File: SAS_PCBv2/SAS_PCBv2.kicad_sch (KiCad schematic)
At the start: 1 part, among them J2 GPIO_CONNECTOR

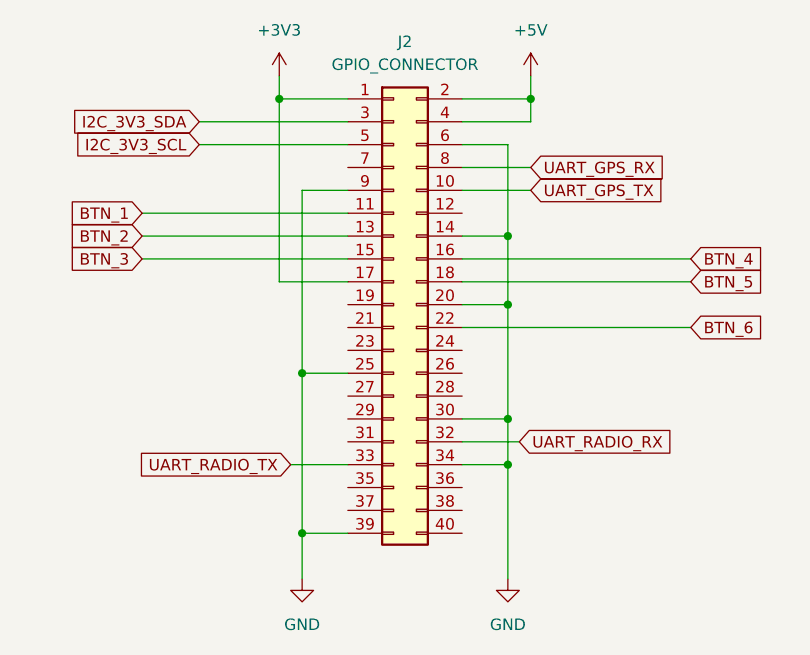
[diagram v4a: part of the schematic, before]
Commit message: schematic sans error et le debut de pcb
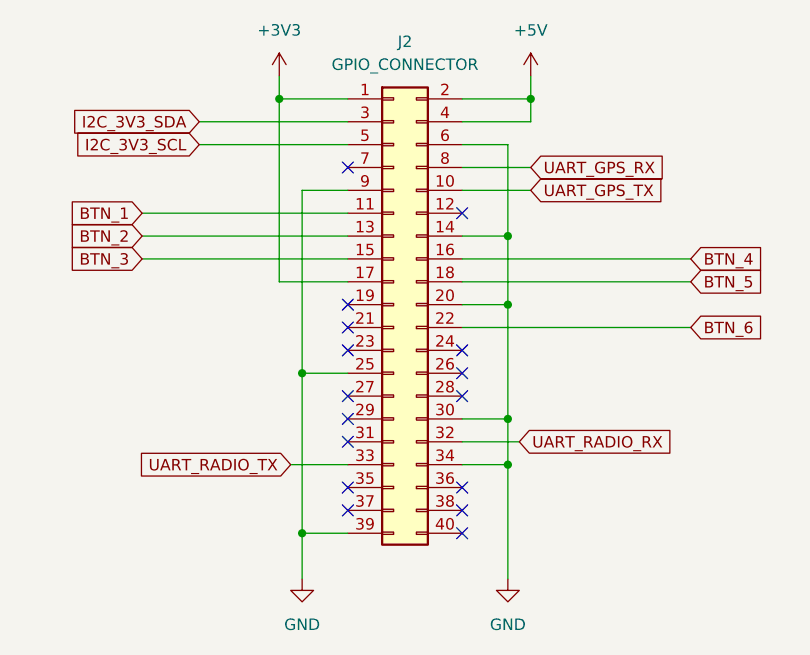
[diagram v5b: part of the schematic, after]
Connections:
- no-connect marks 0 -> 16
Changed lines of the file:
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@@
 		(color 0 0 0 0)
+	)
+	(no_connect
+		(at 179.07 114.3)
+	)
+	(no_connect
+		(at 166.37 88.9)
+	)
+	(no_connect
+		(at 166.37 114.3)
+	)
+	(no_connect
+		(at 179.07 129.54)
+	)
+	(no_connect
+		(at 166.37 119.38)
+	)
+	(no_connect
+		(at 166.37 124.46)
+	)
+	(no_connect
+		(at 166.37 106.68)
+	)
+	(no_connect
+		(at 179.07 124.46)
+	)
+	(no_connect
+		(at 179.07 111.76)
+	)
+	(no_connect
+		(at 179.07 93.98)
+	)
+	(no_connect
+		(at 179.07 109.22)
+	)
+	(no_connect
+		(at 166.37 109.22)
+	)
+	(no_connect
+		(at 166.37 104.14)
+	)
+	(no_connect
+		(at 166.37 116.84)
+	)
+	(no_connect
+		(at 179.07 127)
+	)
+	(no_connect
+		(at 166.37 127)
 	)
 	(wire

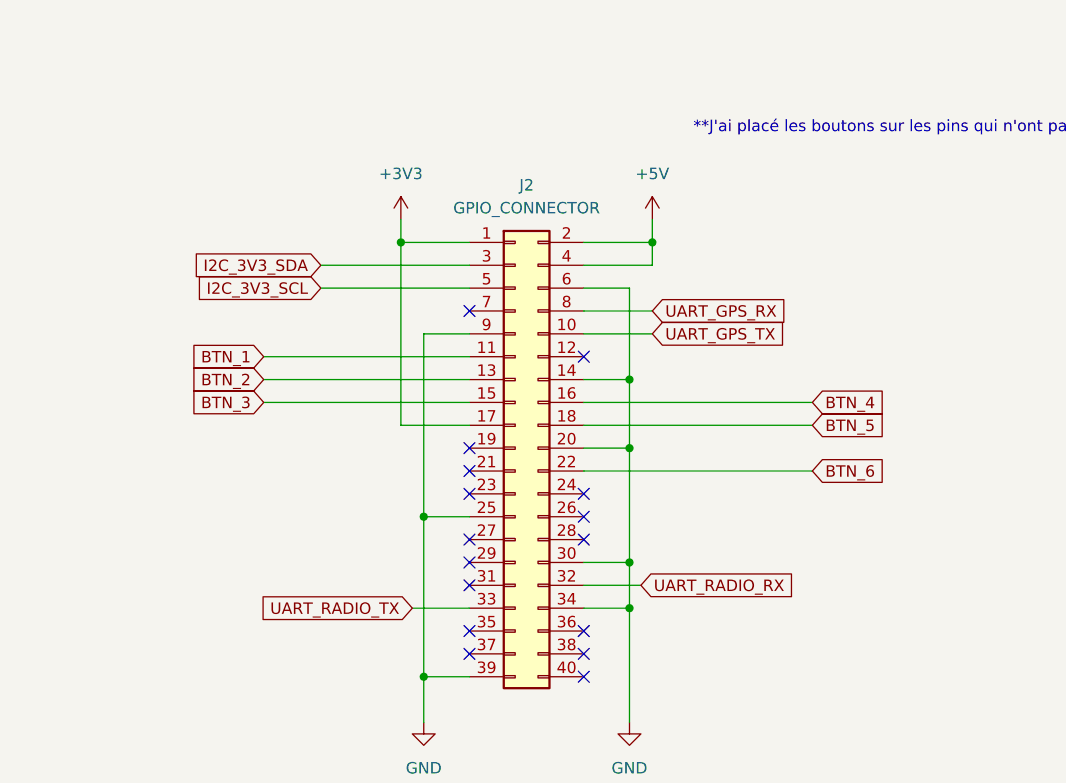
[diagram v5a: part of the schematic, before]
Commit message: Correction UART5 -> UART3, ajout d'un ventilateur 12V PWM
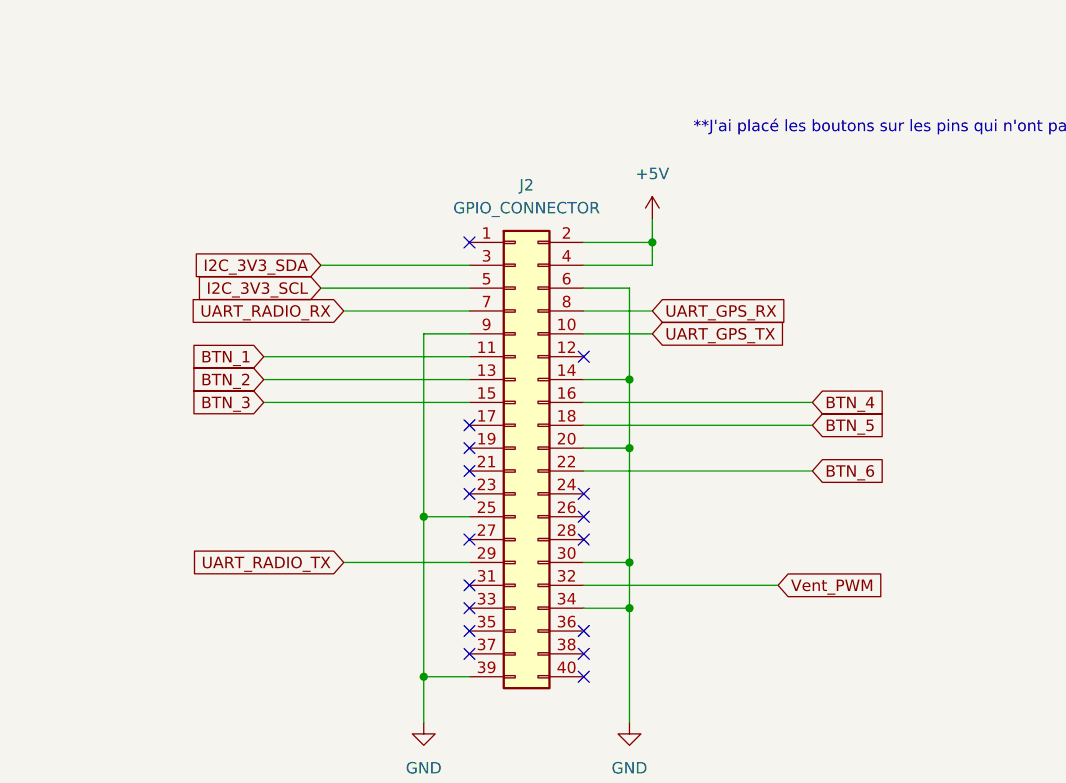
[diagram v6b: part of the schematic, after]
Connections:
- net UART_RADIO_RX: now also J2.7 (Pin_7); no longer J2.32 (Pin_32)
- net UART_RADIO_TX: now also J2.29 (Pin_29); no longer J2.33 (Pin_33)
- net +3V3: no longer names the net of J2.1 (Pin_1)
- net +3V3: no longer J2.17 (Pin_17)
- new net Vent_PWM: J2.32 (Pin_32)
- no-connect marks 16 -> 17
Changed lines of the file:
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@@
 		(color 0 0 0 0)
 	)
-	(junction
-		(at 158.75 81.28)
-		(diameter 0)
-		(color 0 0 0 0)
-	)
 	(no_connect
 		(at 179.07 114.3)
 	)
 	(no_connect
-		(at 166.37 88.9)
-	)
-	(no_connect
 		(at 166.37 114.3)
 	)
@@
 	)
 	(no_connect
-		(at 166.37 116.84)
+		(at 166.37 81.28)
+	)
+	(no_connect
+		(at 166.37 101.6)
 	)
 	(no_connect
@@
 	)
 	(no_connect
+		(at 166.37 121.92)
+	)
+	(no_connect
 		(at 166.37 127)
 	)
@@
 	(wire
 		(pts
-			(xy 160.02 121.92) (xy 166.37 121.92)
-		)
-		(stroke
-			(width 0)
-			(type default)
-		)
-	)
-	(wire
-		(pts
 			(xy 179.07 104.14) (xy 184.15 104.14)
 		)
@@
 	(wire
 		(pts
-			(xy 158.75 81.28) (xy 166.37 81.28)
-		)
-		(stroke
-			(width 0)
-			(type default)
-		)
-	)
-	(wire
-		(pts
 			(xy 149.86 86.36) (xy 166.37 86.36)
 		)
@@
 	(wire
 		(pts
-			(xy 158.75 81.28) (xy 158.75 101.6)
-		)
-		(stroke
-			(width 0)
-			(type default)
-		)
-	)
-	(wire
-		(pts
 			(xy 161.29 111.76) (xy 166.37 111.76)
 		)
@@
 	(wire
 		(pts
+			(xy 152.4 116.84) (xy 166.37 116.84)
+		)
+		(stroke
+			(width 0)
+			(type default)
+		)
+	)
+	(wire
+		(pts
 			(xy 184.15 96.52) (xy 184.15 104.14)
 		)
@@
 	(wire
 		(pts
+			(xy 152.4 88.9) (xy 166.37 88.9)
+		)
+		(stroke
+			(width 0)
+			(type default)
+		)
+	)
+	(wire
+		(pts
 			(xy 161.29 111.76) (xy 161.29 129.54)
 		)
@@
 	(wire
 		(pts
-			(xy 166.37 101.6) (xy 158.75 101.6)
-		)
-		(stroke
-			(width 0)
-			(type default)
-		)
-	)
-	(wire
-		(pts
-			(xy 158.75 78.74) (xy 158.75 81.28)
-		)
-		(stroke
-			(width 0)
-			(type default)
-		)
-	)
-	(wire
-		(pts
 			(xy 143.51 99.06) (xy 166.37 99.06)
 		)
@@
 	(wire
 		(pts
-			(xy 179.07 119.38) (xy 185.42 119.38)
-		)
-		(stroke
-			(width 0)
-			(type default)
-		)
-	)
-	(wire
-		(pts
 			(xy 184.15 121.92) (xy 184.15 134.62)
 		)
@@
 	(wire
 		(pts
+			(xy 179.07 119.38) (xy 200.66 119.38)
+		)
+		(stroke
+			(width 0)
+			(type default)
+		)
+	)
+	(wire
+		(pts
 			(xy 179.07 99.06) (xy 204.47 99.06)
 		)
@@
 	(global_label "UART_RADIO_RX"
 		(shape input)
-		(at 185.42 119.38 0)
+		(at 152.4 88.9 180)
+		(fields_autoplaced yes)
+		(effects
+			(font
+				(size 1.27 1.27)
+			)
+			(justify right)
+		)
+		(property "Intersheetrefs" "${INTERSHEET_REFS}"
+			(at 134.7795 88.9 0)
+			(effects
+				(font
+					(size 1.27 1.27)
+				)
+				(justify right)
+				(hide yes)
+			)
+		)
+	)
+	(global_label "BTN_3"
+		(shape input)
+		(at 143.51 99.06 180)
+		(fields_autoplaced yes)
+		(effects
+			(font
+				(size 1.27 1.27)
+			)
+			(justify right)
+		)
+		(property "Intersheetrefs" "${INTERSHEET_REFS}"
+			(at 134.7796 99.06 0)
+			(effects
+				(font
+					(size 1.27 1.27)
+				)
+				(justify right)
+				(hide yes)
+			)
+		)
+	)
+	(global_label "UART_RADIO_TX"
+		(shape input)
+		(at 152.4 116.84 180)
+		(fields_autoplaced yes)
+		(effects
+			(font
+				(size 1.27 1.27)
+			)
+			(justify right)
+		)
+		(property "Intersheetrefs" "${INTERSHEET_REFS}"
+			(at 135.0819 116.84 0)
+			(effects
+				(font
+					(size 1.27 1.27)
+				)
+				(justify right)
+				(hide yes)
+			)
+		)
+	)
+	(global_label "BTN_5"
+		(shape input)
+		(at 204.47 101.6 0)
 		(fields_autoplaced yes)
 		(effects
@@
 		)
 		(property "Intersheetrefs" "${INTERSHEET_REFS}"
-			(at 203.0405 119.38 0)
+			(at 213.2004 101.6 0)
 			(effects
 				(font
@@
 		)
 	)
-	(global_label "BTN_3"
-		(shape input)
-		(at 143.51 99.06 180)
+	(global_label "BTN_1"
+		(shape input)
+		(at 143.51 93.98 180)
 		(fields_autoplaced yes)
 		(effects
@@
 		)
 		(property "Intersheetrefs" "${INTERSHEET_REFS}"
-			(at 134.7796 99.06 0)
+			(at 134.7796 93.98 0)
 			(effects
 				(font
@@
 		)
 	)
-	(global_label "UART_RADIO_TX"
-		(shape input)
-		(at 160.02 121.92 180)
+	(global_label "I2C_3V3_SDA"
+		(shape input)
+		(at 149.86 83.82 180)
 		(fields_autoplaced yes)
 		(effects
@@
 		)
 		(property "Intersheetrefs" "${INTERSHEET_REFS}"
-			(at 142.7019 121.92 0)
+			(at 134.7796 83.82 0)
 			(effects
 				(font
@@
 		)
 	)
-	(global_label "BTN_5"
-		(shape input)
-		(at 204.47 101.6 0)
+	(global_label "BTN_2"
+		(shape input)
+		(at 143.51 96.52 180)
+		(fields_autoplaced yes)
+		(effects
+			(font
+				(size 1.27 1.27)
+			)
+			(justify right)
+		)
+		(property "Intersheetrefs" "${INTERSHEET_REFS}"
+			(at 134.7796 96.52 0)
+			(effects
+				(font
+					(size 1.27 1.27)
+				)
+				(justify right)
+				(hide yes)
+			)
+		)
+	)
+	(global_label "Vent_PWM"
+		(shape input)
+		(at 200.66 119.38 0)
 		(fields_autoplaced yes)
 		(effects
@@
 		)
 		(property "Intersheetrefs" "${INTERSHEET_REFS}"
-			(at 213.2004 101.6 0)
+			(at 214.4704 119.38 0)
 			(effects
 				(font
@@
 				)
 				(justify left)
-				(hide yes)
-			)
-		)
-	)
-	(global_label "BTN_1"
-		(shape input)
-		(at 143.51 93.98 180)
-		(fields_autoplaced yes)
-		(effects
-			(font
-				(size 1.27 1.27)
-			)
-			(justify right)
-		)
-		(property "Intersheetrefs" "${INTERSHEET_REFS}"
-			(at 134.7796 93.98 0)
-			(effects
-				(font
-					(size 1.27 1.27)
-				)
-				(justify right)
-				(hide yes)
-			)
-		)
-	)
-	(global_label "I2C_3V3_SDA"
-		(shape input)
-		(at 149.86 83.82 180)
-		(fields_autoplaced yes)
-		(effects
-			(font
-				(size 1.27 1.27)
-			)
-			(justify right)
-		)
-		(property "Intersheetrefs" "${INTERSHEET_REFS}"
-			(at 134.7796 83.82 0)
-			(effects
-				(font
-					(size 1.27 1.27)
-				)
-				(justify right)
-				(hide yes)
-			)
-		)
-	)
-	(global_label "BTN_2"
-		(shape input)
-		(at 143.51 96.52 180)
-		(fields_autoplaced yes)
-		(effects
-			(font
-				(size 1.27 1.27)
-			)
-			(justify right)
-		)
-		(property "Intersheetrefs" "${INTERSHEET_REFS}"
-			(at 134.7796 96.52 0)
-			(effects
-				(font
-					(size 1.27 1.27)
-				)
-				(justify right)
 				(hide yes)
 			)
@@
 					(unit 1)
 				)
-			)
-		)
-	)
-	(symbol
-		(lib_id "power:+3V3")
-		(at 158.75 78.74 0)
-		(unit 1)
-		(exclude_from_sim no)
-		(in_bom yes)
-		(on_board yes)
-		(dnp no)
-		(fields_autoplaced yes)
-		(property "Reference" "#PWR032"
-			(at 158.75 82.55 0)
-			(effects
-				(font
-					(size 1.27 1.27)
-				)
-				(hide yes)
-			)
-		)
-		(property "Value" "+3V3"
-			(at 158.75 73.66 0)
-			(effects
-				(font
-					(size 1.27 1.27)
-				)
-			)
-		)
-		(property "Footprint" ""
-			(at 158.75 78.74 0)
-			(effects
-				(font
-					(size 1.27 1.27)
-				)
-				(hide yes)
-			)
-		)
-		(property "Datasheet" ""
-			(at 158.75 78.74 0)
-			(effects
-				(font
-					(size 1.27 1.27)
-				)
-				(hide yes)
-			)
-		)
-		(property "Description" "Power symbol creates a global label with name \"+3V3\""
-			(at 158.75 78.74 0)
-			(effects
-				(font
-					(size 1.27 1.27)
-				)
-				(hide yes)
-			)
-		)
-		(pin "1"
-		)
-		(instances
-			(project ""
-				(path "/9d66b581-dc57-43dc-b827-73e5c0cd12f6"
-					(reference "#PWR032")
-					(unit 1)
-				)

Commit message: Switch USB/PCB, connections Power, spam condensateurs, resistance pull-up
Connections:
- net +5V renamed RPI_5V
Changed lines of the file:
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@@
+	)
+	(junction
+		(at 186.69 83.82)
+		(diameter 0)
+		(color 0 0 0 0)
 	)
 	(junction
@@
 		)
 	)
+	(global_label "RPI_5V"
+		(shape input)
+		(at 186.69 78.74 0)
+		(fields_autoplaced yes)
+		(effects
+			(font
+				(size 1.27 1.27)
+				(color 66 84 255 1)
+			)
+			(justify left)
+		)
+		(property "Intersheetrefs" "${INTERSHEET_REFS}"
+			(at 196.0857 78.74 0)
+			(effects
+				(font
+					(size 1.27 1.27)
+				)
+				(justify left)
+				(hide yes)
+			)
+		)
+	)
 	(global_label "UART_GPS_RX"
 		(shape input)
@@
 				(justify left)
 				(hide yes)
+			)
+		)
+	)
+	(symbol
+		(lib_id "power:PWR_FLAG")
+		(at 186.69 83.82 270)
+		(mirror x)
+		(unit 1)
+		(exclude_from_sim no)
+		(in_bom yes)
+		(on_board yes)
+		(dnp no)
+		(property "Reference" "#FLG06"
+			(at 188.595 83.82 0)
+			(effects
+				(font
+					(size 1.27 1.27)
+				)
+				(hide yes)
+			)
+		)
+		(property "Value" "PWR_FLAG"
+			(at 189.738 83.82 90)
+			(effects
+				(font
+					(size 1.27 1.27)
+				)
+				(justify left)
+			)
+		)
+		(property "Footprint" ""
+			(at 186.69 83.82 0)
+			(effects
+				(font
+					(size 1.27 1.27)
+				)
+				(hide yes)
+			)
+		)
+		(property "Datasheet" "~"
+			(at 186.69 83.82 0)
+			(effects
+				(font
+					(size 1.27 1.27)
+				)
+				(hide yes)
+			)
+		)
+		(property "Description" "Special symbol for telling ERC where power comes from"
+			(at 186.69 83.82 0)
+			(effects
+				(font
+					(size 1.27 1.27)
+				)
+				(hide yes)
+			)
+		)
+		(pin "1"
+		)
+		(instances
+			(project "SAS_PCBv2"
+				(path "/9d66b581-dc57-43dc-b827-73e5c0cd12f6"
+					(reference "#FLG06")
+					(unit 1)
+				)
 			)
 		)
@@
 					(unit 1)
 				)
-			)
-		)
-	)
-	(symbol
-		(lib_id "power:+5V")
-		(at 186.69 78.74 0)
-		(unit 1)
-		(exclude_from_sim no)
-		(in_bom yes)
-		(on_board yes)
-		(dnp no)
-		(fields_autoplaced yes)
-		(property "Reference" "#PWR031"
-			(at 186.69 82.55 0)
-			(effects
-				(font
-					(size 1.27 1.27)
-				)
-				(hide yes)
-			)
-		)
-		(property "Value" "+5V"
-			(at 186.69 73.66 0)
-			(effects
-				(font
-					(size 1.27 1.27)
-				)
-			)
-		)
-		(property "Footprint" ""
-			(at 186.69 78.74 0)
-			(effects
-				(font
-					(size 1.27 1.27)
-				)
-				(hide yes)
-			)
-		)
-		(property "Datasheet" ""
-			(at 186.69 78.74 0)
-			(effects
-				(font
-					(size 1.27 1.27)
-				)
-				(hide yes)
-			)
-		)
-		(property "Description" "Power symbol creates a global label with name \"+5V\""
-			(at 186.69 78.74 0)
-			(effects
-				(font
-					(size 1.27 1.27)
-				)
-				(hide yes)
-			)
-		)
-		(pin "1"
-		)
-		(instances
-			(project ""
-				(path "/9d66b581-dc57-43dc-b827-73e5c0cd12f6"
-					(reference "#PWR031")
-					(unit 1)
-				)

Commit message: LDO du service, Logic level shifter custom
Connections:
- net UART_RAD2_TX: now reaches J2.21 (Pin_21)
- net UART_RAD2_RX: now reaches J2.24 (Pin_24)
- net UART_RADIO_RX renamed UART_RAD1_RX
- net UART_RADIO_TX renamed UART_RAD1_TX
- no-connect marks 17 -> 15
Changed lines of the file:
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@@
-	)
-	(no_connect
-		(at 166.37 106.68)
 	)
 	(no_connect
@@
 	)
 	(no_connect
-		(at 179.07 109.22)
-	)
-	(no_connect
 		(at 166.37 109.22)
 	)
@@
 	(wire
 		(pts
+			(xy 152.4 106.68) (xy 166.37 106.68)
+		)
+		(stroke
+			(width 0)
+			(type default)
+		)
+	)
+	(wire
+		(pts
 			(xy 179.07 106.68) (xy 204.47 106.68)
 		)
@@
 	(wire
 		(pts
+			(xy 179.07 109.22) (xy 196.85 109.22)
+		)
+		(stroke
+			(width 0)
+			(type default)
+		)
+	)
+	(wire
+		(pts
 			(xy 161.29 111.76) (xy 161.29 129.54)
 		)
@@
 		)
 	)
-	(global_label "UART_RADIO_RX"
+	(global_label "UART_RAD1_RX"
 		(shape input)
 		(at 152.4 88.9 180)
@@
 		)
 	)
-	(global_label "UART_RADIO_TX"
+	(global_label "UART_RAD1_TX"
 		(shape input)
 		(at 152.4 116.84 180)
@@
 		)
 	)
+	(global_label "UART_RAD2_TX"
+		(shape input)
+		(at 152.4 106.68 180)
+		(fields_autoplaced yes)
+		(effects
+			(font
+				(size 1.27 1.27)
+			)
+			(justify right)
+		)
+		(property "Intersheetrefs" "${INTERSHEET_REFS}"
+			(at 135.0819 106.68 0)
+			(effects
+				(font
+					(size 1.27 1.27)
+				)
+				(justify right)
+				(hide yes)
+			)
+		)
+	)
 	(global_label "UART_GPS_TX"
 		(shape input)
@@
 		(property "Intersheetrefs" "${INTERSHEET_REFS}"
 			(at 196.0857 78.74 0)
+			(effects
+				(font
+					(size 1.27 1.27)
+				)
+				(justify left)
+				(hide yes)
+			)
+		)
+	)
+	(global_label "UART_RAD2_RX"
+		(shape input)
+		(at 196.85 109.22 0)
+		(fields_autoplaced yes)
+		(effects
+			(font
+				(size 1.27 1.27)
+			)
+			(justify left)
+		)
+		(property "Intersheetrefs" "${INTERSHEET_REFS}"
+			(at 214.4705 109.22 0)
 			(effects
 				(font
@@
 			(at 171.45 104.14 0)
 			(effects
+				(font
+					(size 1.27 1.27)
+				)
+				(hide yes)
+			)
+		)
+		(property "AVAILABILITY" ""
+			(at 171.45 104.14 0)
+			(effects
+				(font
+					(size 1.27 1.27)
+				)
+				(hide yes)
+			)
+		)
+		(property "Digikey" ""
+			(at 171.45 104.14 0)
+			(effects
+				(font
+					(size 1.27 1.27)
+				)
+				(hide yes)
+			)
+		)
+		(property "MF" ""
+			(at 171.45 104.14 0)
+			(effects
+				(font
+					(size 1.27 1.27)
+				)
+				(hide yes)
+			)
+		)
+		(property "MP" ""
+			(at 171.45 104.14 0)
+			(effects
+				(font
+					(size 1.27 1.27)
+				)
+				(hide yes)
+			)
+		)
+		(property "PACKAGE" ""
+			(at 171.45 104.14 0)
+			(effects
+				(font
+					(size 1.27 1.27)
+				)
+				(hide yes)
+			)
+		)
+		(property "PRICE" ""
+			(at 171.45 104.14 0)
+			(effects
+				(font
+					(size 1.27 1.27)
+				)
+				(hide yes)
+			)
+		)
+		(property "PURCHASE-URL" ""
+			(at 171.45 104.14 0)
+			(effects
